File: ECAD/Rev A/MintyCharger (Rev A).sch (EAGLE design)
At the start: 73 parts, among them IC1 74HC595D, IC2 74HC595D, Q1 IRLML6346TRPBF, Q2 NTD18N06LT4G, U1 LM258ADR, U2 LM258ADR, U3 PIC16F18325-I/SL

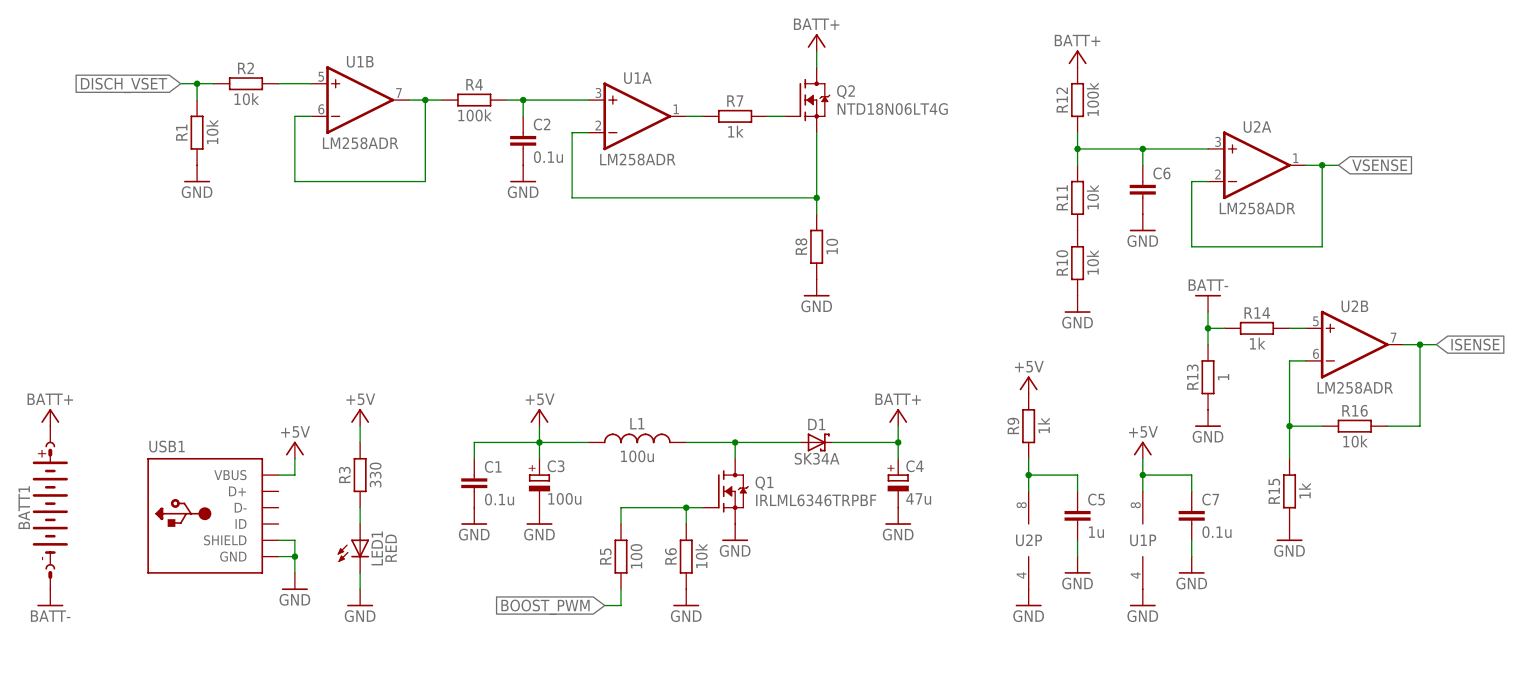
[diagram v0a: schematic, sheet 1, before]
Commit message: Finished the board layout of RevA
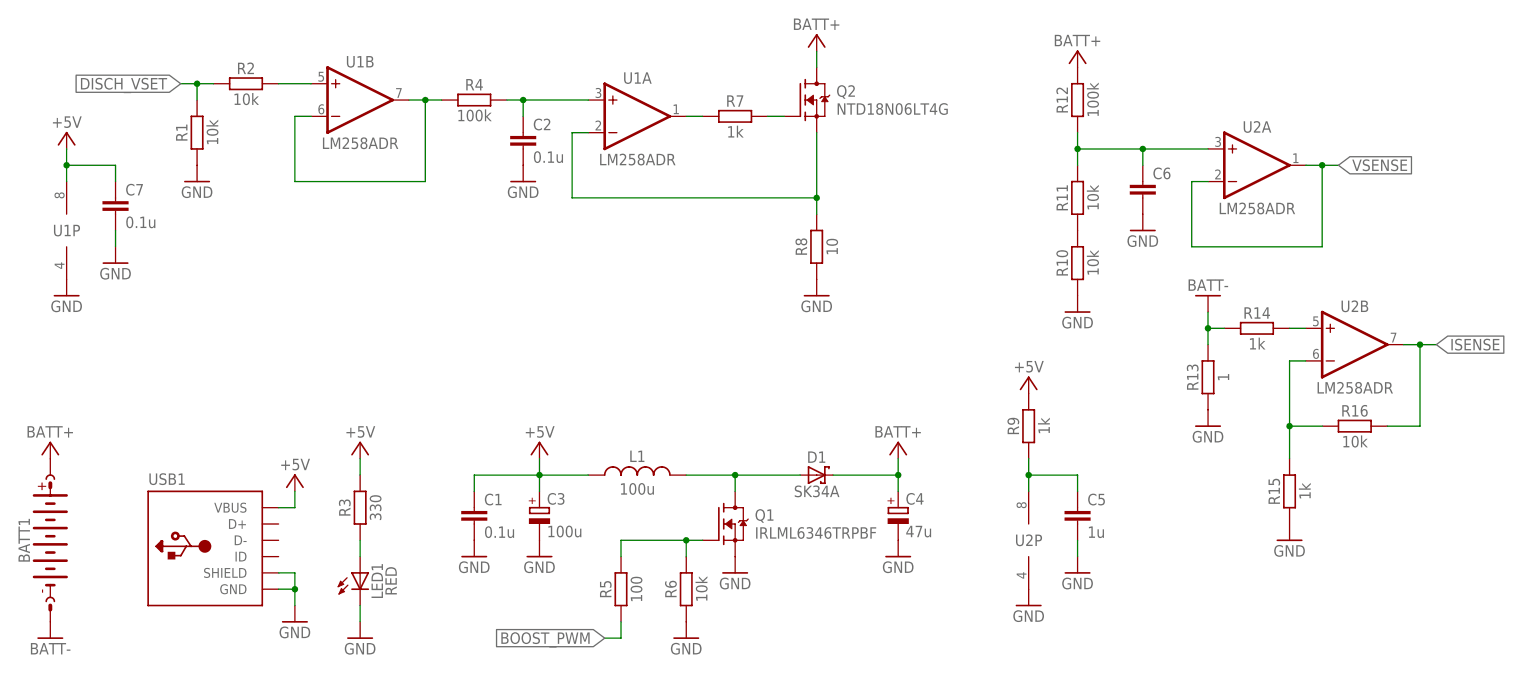
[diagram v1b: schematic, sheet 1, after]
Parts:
- BATT1: device innove-holders:KEYSTONE-590-9V -> innove-batteries:KEYSTONE-590-9V
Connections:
- net N$28: no longer S1.P1
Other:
- moved on the sheet: BATT1, C1, C3, C4, C7, D1, L1, LED1, Q1, R3, R5, R6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
